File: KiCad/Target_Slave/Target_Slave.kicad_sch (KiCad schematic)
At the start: 23 parts, among them J1 RJ11 Header, J3 RJ11 Header, U1 PIC16F1788-IP, U2 TSOP32238, U3 TSOP53456

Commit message: Finalized schematics
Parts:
- C1: value 1uF -> 22uF
- C2: value 1uF -> 0.1uF
- J1, J3: value RJ11 Header -> ~; footprint AlexWheelockFootprintLibrary:RJ11_Connector -> (none)
- U2: footprint OptoDevice:Vishay_MOLD-3Pin -> (none)
- U3: footprint OptoDevice:Vishay_MINIMOLD-3Pin -> (none)
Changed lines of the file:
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@@
 	(title_block
 		(title "Laser Arcade Slave")
-		(date "2025-04-01")
+		(date "2025-04-14")
 		(rev "A")
 		(company "Idaho State University")
@@
 	(text "I2C"
 		(exclude_from_sim no)
-		(at 106.426 148.336 0)
+		(at 112.014 141.478 0)
 		(effects
 			(font
@@
 	(text "RC3, Pin 2 = SCL\nRC4, Pin 3 = SDA"
 		(exclude_from_sim no)
-		(at 122.428 151.638 0)
+		(at 128.016 144.78 0)
 		(effects
 			(font
@@
 	(text "I2C"
 		(exclude_from_sim no)
-		(at 39.624 148.336 0)
+		(at 35.052 141.478 0)
 		(effects
 			(font
@@
 	(text "RC3, Pin 2 = SCL\nRC4, Pin 3 = SDA"
 		(exclude_from_sim no)
-		(at 23.876 151.638 0)
+		(at 19.304 144.78 0)
 		(effects
 			(font
@@
 			)
 		)
-		(property "Value" "1uF"
+		(property "Value" "0.1uF"
 			(at 63.5 160.0262 0)
 			(effects
@@
 			)
 		)
-		(property "Footprint" "OptoDevice:Vishay_MOLD-3Pin"
+		(property "Footprint" ""
 			(at 215.9 102.235 0)
 			(effects
@@
 			)
 		)
-		(property "Value" "RJ11 Header"
+		(property "Value" "~"
 			(at 35.052 145.796 0)
 			(effects
@@
 			)
 		)
-		(property "Footprint" "AlexWheelockFootprintLibrary:RJ11_Connector"
+		(property "Footprint" ""
 			(at 44.45 134.62 0)
 			(effects
@@
 			)
 		)
-		(property "Value" "RJ11 Header"
+		(property "Value" "~"
 			(at 110.998 145.796 0)
 			(effects
@@
 			)
 		)
-		(property "Footprint" "AlexWheelockFootprintLibrary:RJ11_Connector"
+		(property "Footprint" ""
 			(at 101.6 134.62 0)
 			(effects
@@
 		(on_board yes)
 		(dnp no)
-		(fields_autoplaced yes)
 		(property "Reference" "C1"
-			(at 52.07 157.4862 0)
+			(at 52.324 157.48 0)
 			(effects
 				(font
@@
 			)
 		)
-		(property "Value" "1uF"
-			(at 52.07 160.0262 0)
+		(property "Value" "22uF"
+			(at 52.324 160.02 0)
 			(effects
 				(font
@@
 			)
 		)
-		(property "Footprint" "OptoDevice:Vishay_MINIMOLD-3Pin"
+		(property "Footprint" ""
 			(at 215.9 130.175 0)
 			(effects

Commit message: Target Slave PCB
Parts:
- removed D6: ~, symbol Libraries:RGB_LED_P32TRRRGB
- removed U2: TSOP32238, symbol Interface_Optical:TSOP321xx
- added D2: IN-P32TRRRGB, 0_AKeller_Footprints:IN-P32TRRRGB, symbol Libraries:RGB_LED_P32TRRRGB
- added R1, R2, R6, R7, R8: 330Ω, Resistor_SMD:R_0805_2012Metric_Pad1.20x1.40mm_HandSolder, symbol Libraries:R_Custom
- added R10, R12: 90Ω, Resistor_SMD:R_0805_2012Metric_Pad1.20x1.40mm_HandSolder, symbol Libraries:R_Custom
- added R11: 150Ω, Resistor_SMD:R_0805_2012Metric_Pad1.20x1.40mm_HandSolder, symbol Libraries:R_Custom
- added SW1: I2C Address, 0_AKeller_Footprints:SW_DIP_SPSTx08_Slide_9.78x22.5mm_W7.62mm_P2.54mm, symbol Switch:SW_DIP_x08
- added U2: TSSP4038, 0_AKeller_Footprints:IR Receiver, symbol Interface_Optical:TSOP331xx
- D1: renamed from D2; footprint Diode_SMD:D_0805_2012Metric_Pad1.15x1.40mm_HandSolder -> 0_AKeller_Footprints:Diode_0805
- D3, D4, D5: value ~ -> IN-P32TRRRGB; footprint (none) -> 0_AKeller_Footprints:IN-P32TRRRGB
- J1: renamed from J2; value ~ -> ICSP; footprint Connector_PinHeader_2.54mm:PinHeader_1x05_P2.54mm_Vertical -> 0_AKeller_Footprints:1x6_100mil_Header; symbol Libraries:Header_1x5 -> 0_AKeller_Parts:Header_1x6
- J2: renamed from J1; value ~ -> I2C; footprint (none) -> 0_AKeller_Footprints:1x4_100mil_Header
- J3: value ~ -> I2C; footprint (none) -> 0_AKeller_Footprints:1x4_100mil_Header
- R3, R5: value 90Ω -> 330Ω; footprint (none) -> Resistor_SMD:R_0805_2012Metric_Pad1.20x1.40mm_HandSolder
- R4: value 150Ω -> 330Ω; footprint (none) -> Resistor_SMD:R_0805_2012Metric_Pad1.20x1.40mm_HandSolder
- U1: footprint (none) -> 0_AKeller_Footprints:SSOP-28
- U3: footprint (none) -> 0_AKeller_Footprints:IR Receiver
- renumbered C4 to C1, C3 to C2, C5 to C3, C6 to C4, C1 to C5, C2 to C6, D1 to D6, R2 to R13, R1 to R9
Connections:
- net +5V: now also D2.4 (A), SW1.1, SW1.2, SW1.3, SW1.4, SW1.5, SW1.6, SW1.7, SW1.8, U2.3 (Vs)
- net GND: now also C1.1, C2.2, C3.2, C4.2, C5.2, C6.2, J1.3, R13.1, R3.1, R4.1, R5.1, R1.1, R2.1, R6.1, R7.1, R8.1, U2.2 (GND)
- net RB6: now also U1.27 (ICSPCLK/RB6); no longer U1.17 (RC6/TX/CK)
- net RB7: now also U1.28 (ICSPDAT/RB7); no longer U1.18 (RC7/RX/DT)
- net at U1.21 (INT/AN12/RB0): now also U2.1 (OUT)
- net RA6: now reaches U1.10 (CLKOUT/OSC2/RA6)
- net RA6: now also R7.2, SW1.10
- net RA0: now reaches U1.2 (ULPWU/C12IN0-/AN0/RA0)
- net RA0: now also R1.2, SW1.16; no longer R3.1
- net at U1.23 (P1B/AN8/RB2): now also R12.1
- net at U1.24 (PGM/C12IN2-/AN8/RB3): now also R11.2
- net at U1.25 (P1D/AN11/RB4): now also R10.2
- net RA1: now reaches U1.3 (C12IN1-/AN1/RA1)
- net RA1: now also R2.2, SW1.15; no longer R4.1
- net RA2: now reaches U1.4 (CVref/C2IN1+/Vref-/AN2/RA2)
- net RA2: now also R3.2, SW1.14; no longer R5.1
- net RA3: now reaches U1.5 (C1IN+/Vref+/AN3/RA3)
- net RA3: now also R4.2, SW1.13
- net RA4: now reaches U1.6 (T0CKI/C1OUT/RA4)
- net RA4: now also R5.2, SW1.12
- net RA5: now reaches U1.7 (~{SS}/C2OUT/AN4/RA5)
- net RA5: now also R6.2, SW1.11
- net RA7: now reaches U1.9 (CLKIN/OSC1/RA7)
- net RA7: now also R8.2, SW1.9
- net at D3.1 (BK), D4.1 (BK), D5.1 (BK): now also D2.1 (BK), R10.1; no longer R5.2
- net at D3.2 (GK), D4.2 (GK), D5.2 (GK): now also D2.2 (GK), R12.2; no longer R3.2
- net at D3.3 (RK), D4.3 (RK), D5.3 (RK): now also D2.3 (RK), R11.1; no longer R4.2
- no-connect marks 15 -> 8

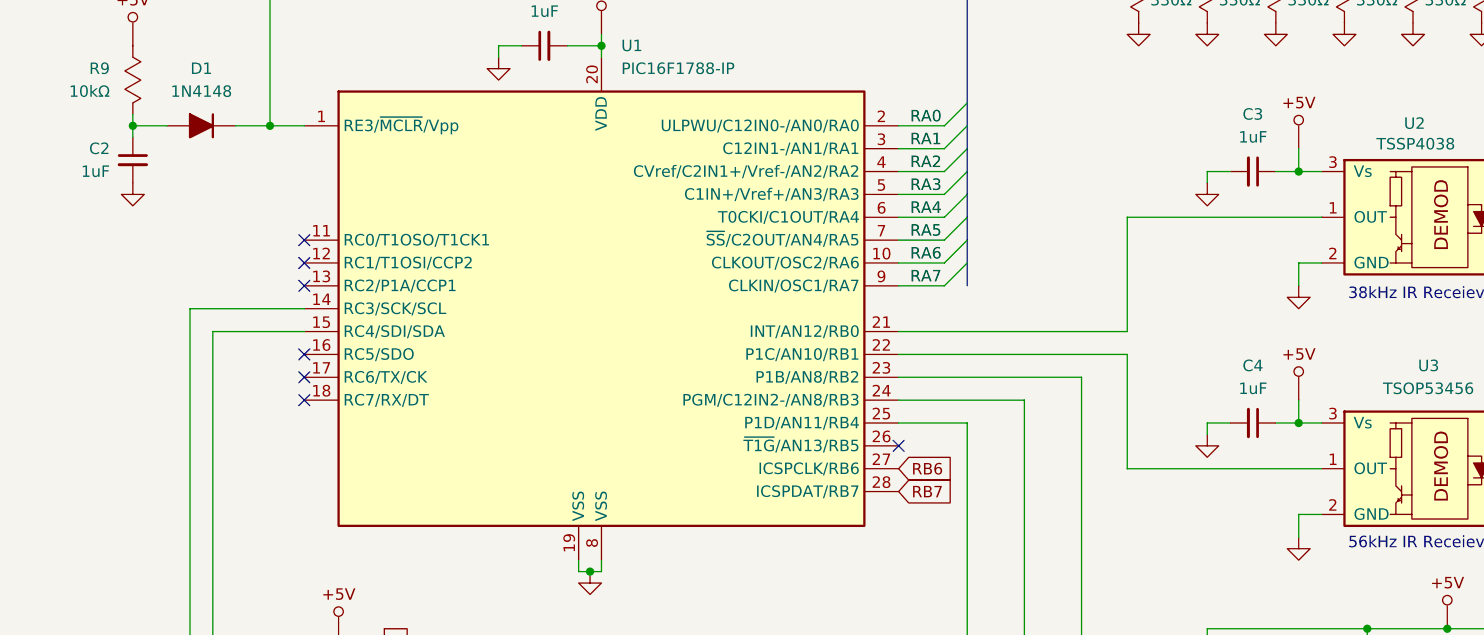
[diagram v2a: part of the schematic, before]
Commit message: Master PCB design, Slave board logos
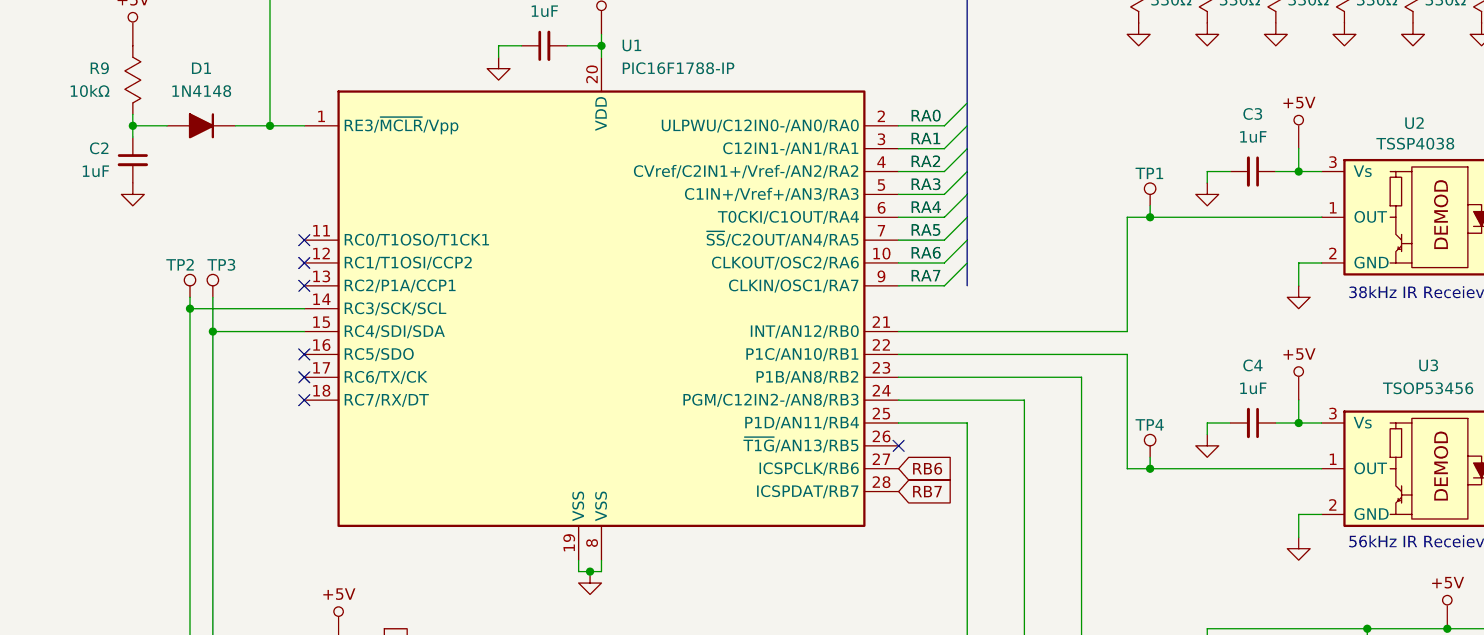
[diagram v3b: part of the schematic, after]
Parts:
- added TP1, TP2, TP3, TP4: ~, 0_AKeller_Footprints:1x1_100mil_Header, symbol 0_AKeller_Parts:Test_Point
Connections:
- net at J2.2, J3.2, U1.14 (RC3/SCK/SCL): now also TP2.1
- net at J2.3, J3.3, U1.15 (RC4/SDI/SDA): now also TP3.1
- net at U1.21 (INT/AN12/RB0), U2.1 (OUT): now also TP1.1
- net at U1.22 (P1C/AN10/RB1), U3.1 (OUT): now also TP4.1

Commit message: Master board silkscreen and gerber files
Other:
- moved on the sheet: C1, C2, C3, C4, C5, C6, D1, D2, D3, D4, D5, D6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
